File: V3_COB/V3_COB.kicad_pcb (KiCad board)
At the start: 4 copper layers, 18 x 16 mm, 3 parts, among them J1 Conn_2Rows-76Pins, J101 Conn_02x35_Counter_Clockwise_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

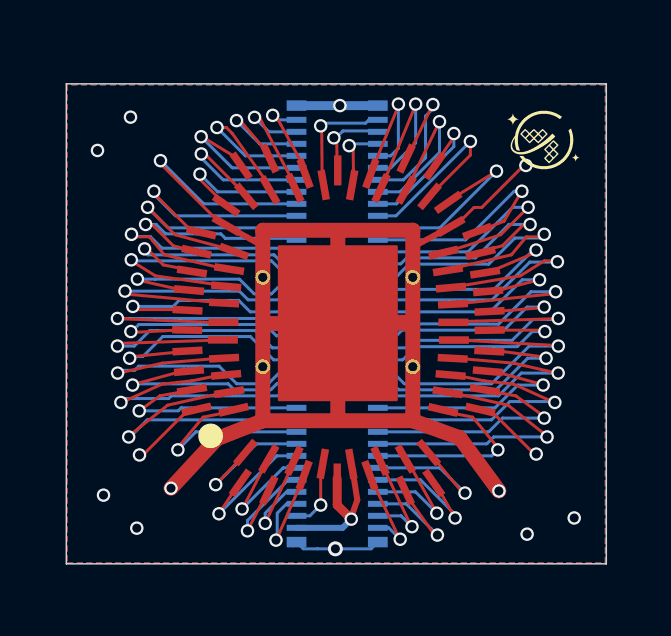
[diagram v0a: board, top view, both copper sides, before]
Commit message: V3_COB clean up
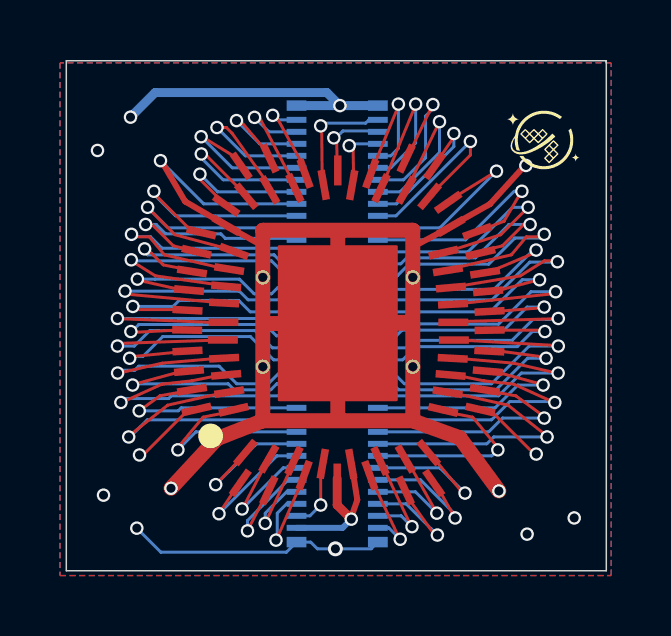
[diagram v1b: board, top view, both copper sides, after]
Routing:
- net GND: track 22.8 -> 29.8 mm
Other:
- board size 18 x 16 mm -> 18 x 17 mm
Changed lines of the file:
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@@
 		(grid_origin 180 65)
 		(pcbplotparams
-			(layerselection 0x00000000_00000000_55555555_5755f5ff)
-			(plot_on_all_layers_selection 0x00000000_00000000_00000000_00000000)
+			(layerselection 0x00000000_00000000_5555555f_fff5ffff)
+			(plot_on_all_layers_selection 0x00000000_00000000_0000000a_aaa0aaff)
 			(disableapertmacros no)
 			(usegerberextensions no)
@@
 			(outputformat 1)
 			(mirror no)
-			(drillshape 1)
+			(drillshape 0)
 			(scaleselection 1)
-			(outputdirectory "")
+			(outputdirectory "Gerber_Drill_Files/")
 		)
 	)
@@
 	)
 	(gr_line
+		(start 208.22 60.09)
+		(end 209.25 59.51)
+		(stroke
+			(width 0.2)
+			(type default)
+		)
+		(layer "F.Cu")
+		(net 55)
+	)
+	(gr_line
 		(start 208.25 67.3)
 		(end 209.55 69.07)
@@
 	)
 	(gr_line
+		(start 199.09 59.42)
+		(end 198.33 58.12)
+		(stroke
+			(width 0.2)
+			(type default)
+		)
+		(layer "F.Cu")
+		(net 55)
+	)
+	(gr_line
 		(start 200.17 64.65)
 		(end 198.33 64.81)
@@
 	)
 	(gr_line
+		(start 200.17 60.05)
+		(end 199.09 59.42)
+		(stroke
+			(width 0.2)
+			(type default)
+		)
+		(layer "F.Cu")
+		(net 55)
+	)
+	(gr_line
 		(start 200.25 65.21)
 		(end 199.31 65.4)
@@
 	)
 	(gr_line
+		(start 209.25 59.51)
+		(end 210.39 58.25)
+		(stroke
+			(width 0.2)
+			(type default)
+		)
+		(layer "F.Cu")
+		(net 55)
+	)
+	(gr_line
 		(start 200.3 62.8)
 		(end 197.04 62.5)
@@
 	)
 	(gr_rect
-		(start 195.13 55.5)
-		(end 213.13 71.5)
+		(start 195.13 54.73)
+		(end 213.13 71.73)
 		(stroke
 			(width 0.05)
-			(type default)
+			(type solid)
 		)
 		(fill no)
@@
 	(dimension
 		(type orthogonal)
-		(layer "Eco1.User")
+		(layer "User.1")
 		(pts
-			(xy 212.34 71.5) (xy 212.16 55.5)
+			(xy 213.13 71.73) (xy 213.13 54.73)
 		)
-		(height 2.18)
+		(height 3.87)
 		(orientation 1)
 		(format
@@
 			(units 3)
 			(units_format 1)
-			(precision 0)
+			(precision 4)
 		)
 		(style
 			(thickness 0.1)
 			(arrow_length 1.27)
-			(text_position_mode 2)
+			(text_position_mode 0)
 			(arrow_direction outward)
 			(extension_height 0.58642)
@@
 			(keep_text_aligned yes)
 		)
-		(gr_text "16 mm"
-			(at 215.57 63.589947 90)
-			(layer "Eco1.User")
+		(gr_text "17.0000 mm"
+			(at 215.85 63.23 90)
+			(layer "User.1")
 			(effects
 				(font
@@
 	)
 	(segment
-		(start 200.325 60.215)
-		(end 198.27 58.16)
-		(width 0.1)
-		(layer "F.Cu")
-		(net 55)
-	)
-	(segment
 		(start 210.45 58.26)
 		(end 210.45 58.22)
@@
 	)
 	(segment
-		(start 208.085 60.255)
-		(end 208.72 59.62)
-		(width 0.1)
-		(layer "F.Cu")
-		(net 55)
-	)
-	(segment
-		(start 208.72 59.62)
-		(end 208.98 59.62)
-		(width 0.1)
-		(layer "F.Cu")
-		(net 55)
-	)
-	(segment
 		(start 199.205 66.355)
 		(end 197.69 67.87)
@@
 	)
 	(segment
-		(start 208.98 59.62)
-		(end 210.38 58.22)
-		(width 0.1)
-		(layer "F.Cu")
-		(net 55)
-	)
-	(segment
 		(start 199.47 66.355)
 		(end 199.205 66.355)
@@
 	)
 	(segment
-		(start 203.029 70.999)
-		(end 203.5 70.999)
+		(start 202.805 56.225)
+		(end 202.694 56.114)
 		(width 0.1)
 		(layer "B.Cu")
@@
 	)
 	(segment
-		(start 202.805 56.225)
-		(end 202.694 56.114)
+		(start 198.09 55.79)
+		(end 197.27 56.61)
+		(width 0.3)
+		(layer "B.Cu")
+		(net 55)
+	)
+	(segment
+		(start 198.281 71.111)
+		(end 197.48 70.31)
 		(width 0.1)
 		(layer "B.Cu")
@@
 	)
 	(segment
+		(start 203.276 70.775)
+		(end 203.5 70.999)
+		(width 0.1)
+		(layer "B.Cu")
+		(net 55)
+	)
+	(segment
 		(start 205.291 70.999)
 		(end 205.515 70.775)
@@
 	)
 	(segment
-		(start 202.805 70.775)
-		(end 202.674503 70.905497)
+		(start 202.805 59.5)
+		(end 199.71 59.5)
 		(width 0.1)
 		(layer "B.Cu")
@@
 	)
 	(segment
-		(start 202.805 59.5)
-		(end 199.71 59.5)
-		(width 0.1)
+		(start 203.815 55.79)
+		(end 198.09 55.79)
+		(width 0.3)
 		(layer "B.Cu")
 		(net 55)
@@
 	(segment
 		(start 202.805 70.775)
-		(end 203.029 70.999)
+		(end 202.469 71.111)
 		(width 0.1)
 		(layer "B.Cu")
@@
 	)
 	(segment
+		(start 202.805 70.775)
+		(end 203.276 70.775)
+		(width 0.1)
+		(layer "B.Cu")
+		(net 55)
+	)
+	(segment
 		(start 202.86 56.17)
 		(end 202.805 56.225)
@@
 	)
 	(segment
+		(start 202.469 71.111)
+		(end 198.281 71.111)
+		(width 0.1)
+		(layer "B.Cu")
+		(net 55)
+	)
+	(segment
+		(start 204.25 56.225)
+		(end 203.815 55.79)
+		(width 0.3)
+		(layer "B.Cu")
+		(net 55)
+	)
+	(segment
 		(start 199.71 59.5)
 		(end 198.27 58.06)
@@
 		(polygon
 			(pts
-				(xy 195.16 55.53) (xy 195.16 71.47) (xy 213.1 71.47) (xy 213.1 55.53)
+				(xy 194.92 54.8) (xy 194.92 71.89) (xy 213.29 71.89) (xy 213.29 54.8)
 			)
 		)
